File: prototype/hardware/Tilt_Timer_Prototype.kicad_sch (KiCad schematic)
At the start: 11 parts, among them Q1 PNP, Q2 PNP, Q3 PNP, Q4 PNP, U1 RPi5 GPIO Extension Shield, U2 MPU6050 Module, U3 74HC595

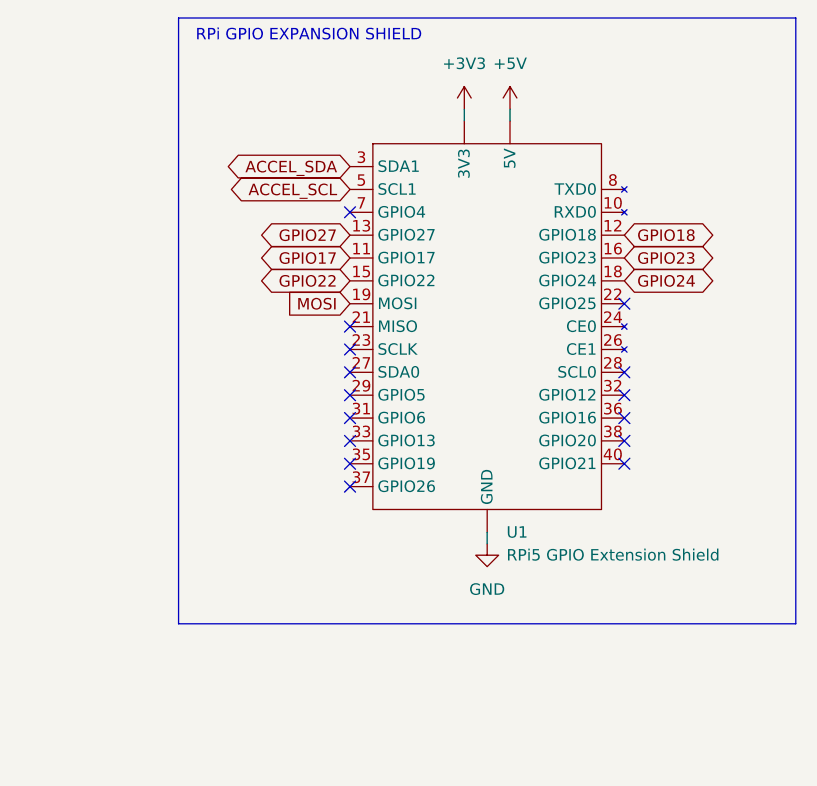
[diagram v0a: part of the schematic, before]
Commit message: replaced rpi with esp32
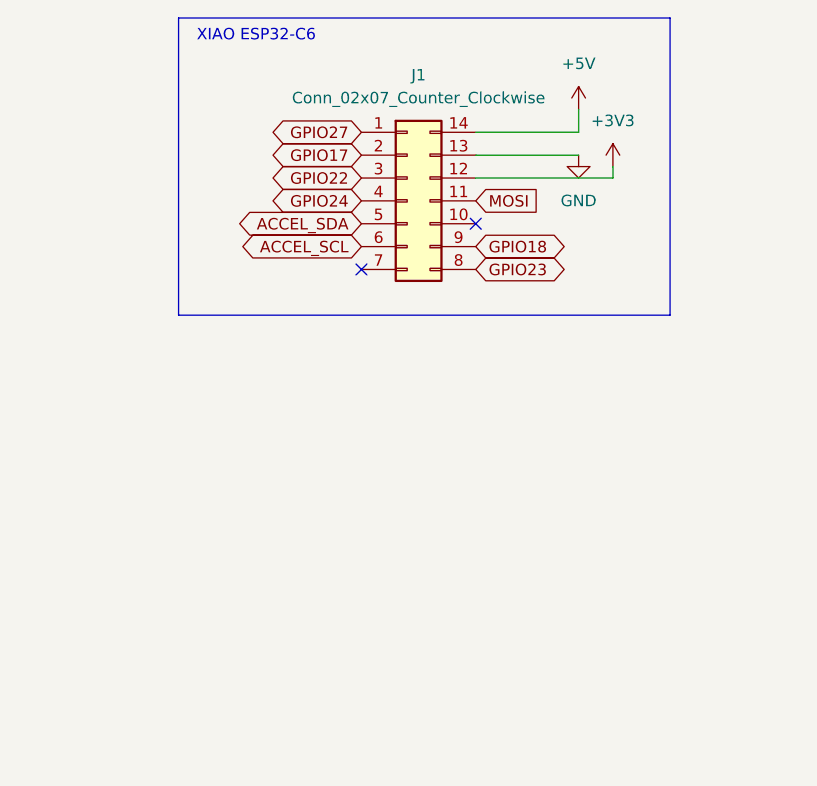
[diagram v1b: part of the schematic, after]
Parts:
- removed U1: RPi5 GPIO Extension Shield, symbol Prototype_Parts:RPi5_GPIO_Extension_Shield
- added J1: Conn_02x07_Counter_Clockwise, symbol Connector_Generic:Conn_02x07_Counter_Clockwise
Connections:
- net +3V3: now also J1.12 (Pin_12)
- net +5V: now also J1.14 (Pin_14)
- net ACCEL_SCL: now also J1.6 (Pin_6)
- net ACCEL_SDA: now also J1.5 (Pin_5)
- net GND: now also J1.13 (Pin_13)
- net GPIO17: now also J1.2 (Pin_2)
- net GPIO18: now also J1.9 (Pin_9)
- net GPIO22: now also J1.3 (Pin_3)
- net GPIO23: now also J1.8 (Pin_8)
- net GPIO24: now also J1.4 (Pin_4)
- net GPIO27: now also J1.1 (Pin_1)
- net MOSI: now also J1.11 (Pin_11)
- no-connect marks 16 -> 3
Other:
- note added: "XIAO ESP32-C6"
- note removed: "RPi GPIO EXPANSION SHIELD"
